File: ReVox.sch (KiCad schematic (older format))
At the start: 45 parts, among them CN1 EXPANSION_PORT, CN2 AUDIO_OUT, CN3 AUDIO_OUT, CN4 CN_RAW_DAC, U1 GAL20V8, U2 74LS273, U3 LM386

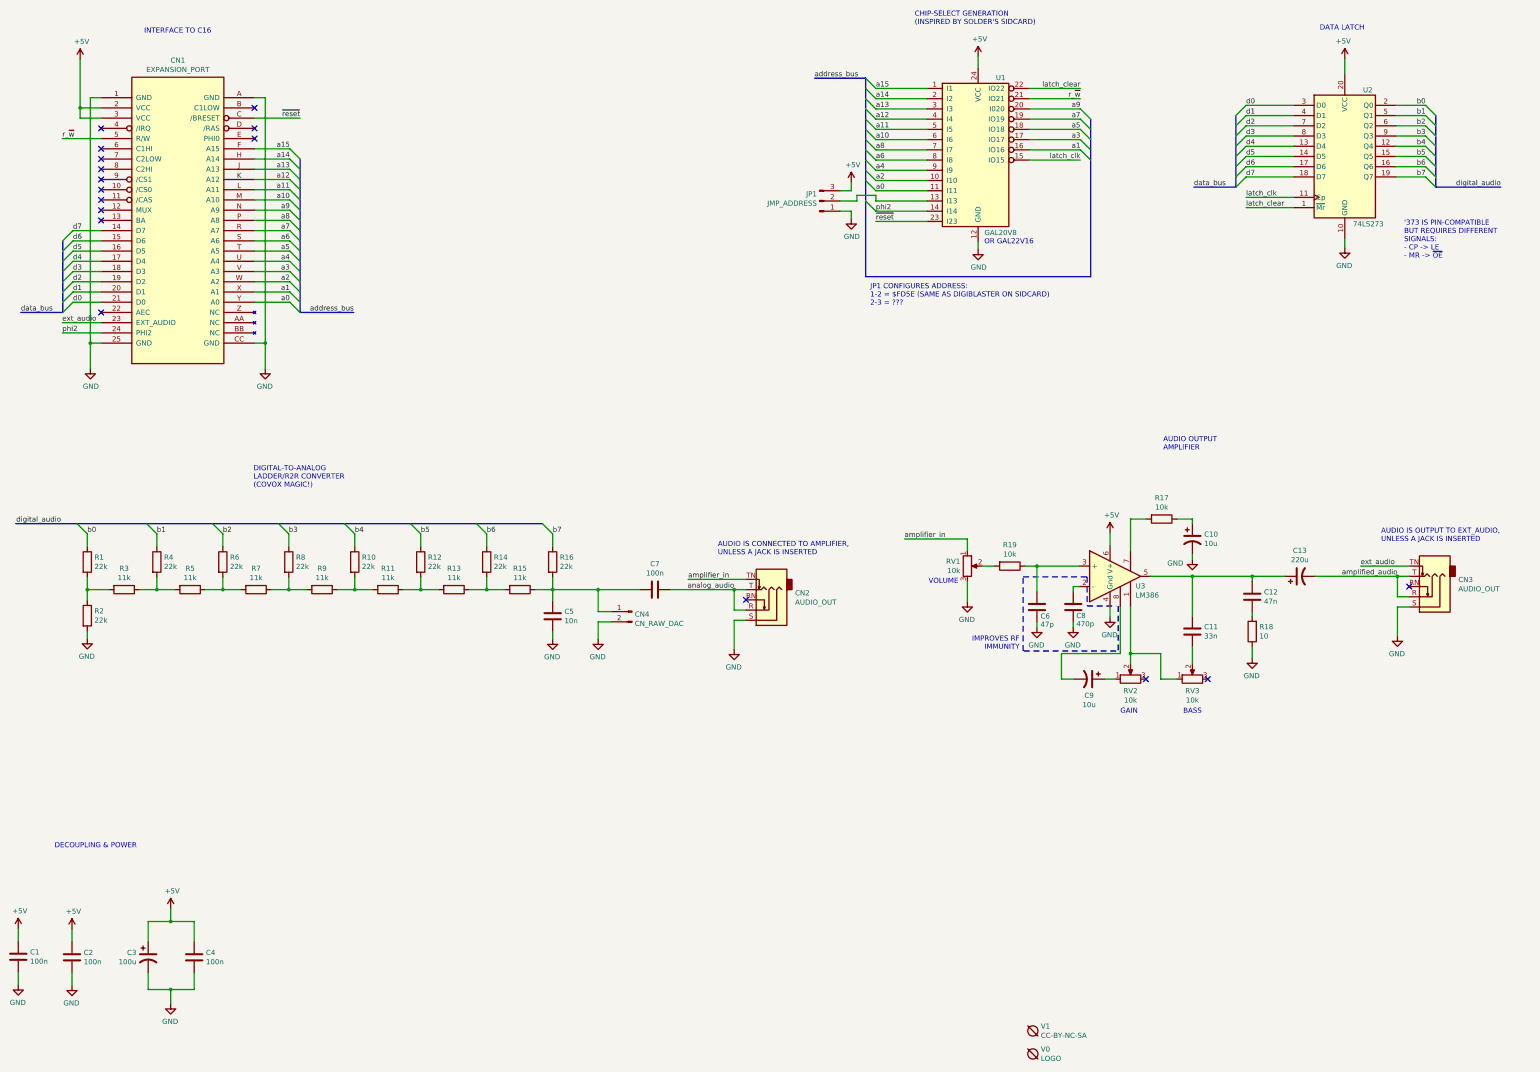
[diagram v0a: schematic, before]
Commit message: Simpler amplifier circuit
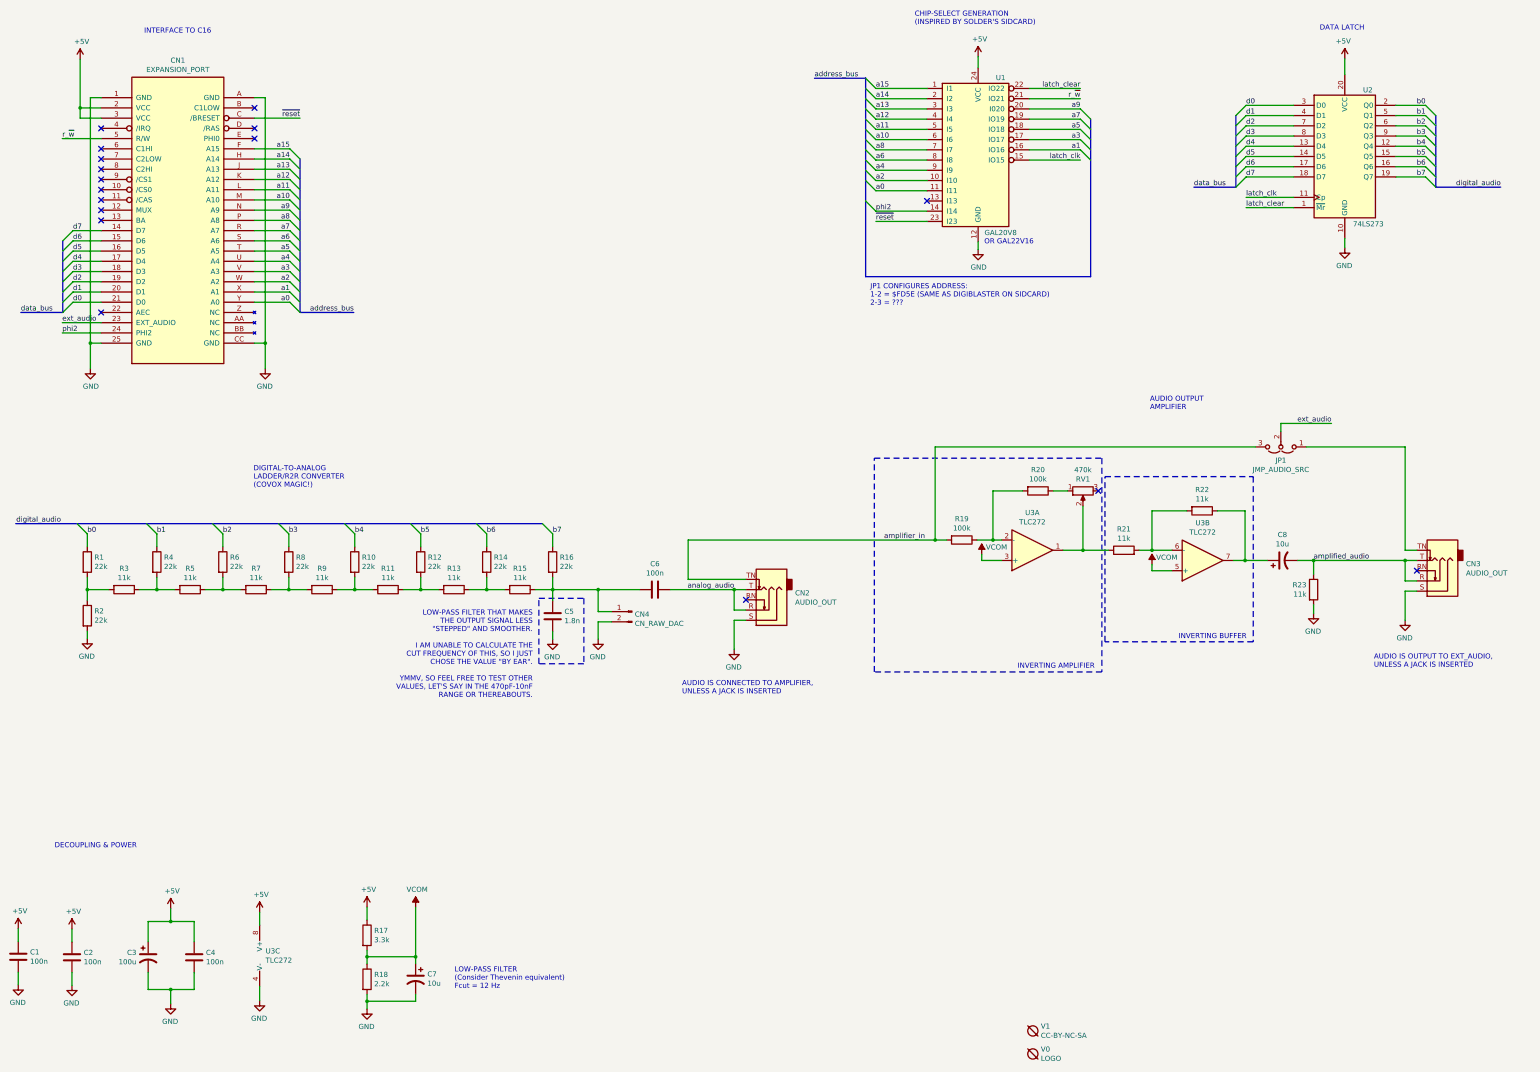
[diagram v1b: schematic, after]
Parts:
- removed C10, C9: 10u, Capacitor_THT:CP_Radial_D5.0mm_P2.00mm, symbol Device:CP1
- removed C11: 33n, Capacitor_THT:C_Disc_D7.0mm_W2.5mm_P5.00mm, symbol Device:C
- removed C12: 47n, Capacitor_THT:C_Disc_D7.0mm_W2.5mm_P5.00mm, symbol Device:C
- removed C13: 220u, Capacitor_THT:CP_Radial_D8.0mm_P3.50mm, symbol Device:CP1
- removed C6: 47p, Capacitor_THT:C_Disc_D7.0mm_W2.5mm_P5.00mm, symbol Device:C
- removed C8: 470p, Capacitor_THT:C_Disc_D7.0mm_W2.5mm_P5.00mm, symbol Device:C
- removed JP1: JMP_ADDRESS, Connector_PinHeader_2.54mm:PinHeader_1x03_P2.54mm_Vertical, symbol Connector:Conn_01x03_Male
- removed RV1, RV3: 10k, ReVox:Pot_Bourns_3306P, symbol Device:R_POT
- removed U3: LM386, Package_DIP:DIP-8_W7.62mm_Socket_LongPads, symbol lm386-mod-pin7:LM386
- added C7, C8: 10u, Capacitor_THT:CP_Radial_D5.0mm_P2.00mm, symbol Device:CP1
- added JP1: JMP_AUDIO_SRC, Jumper:SolderJumper-3_P1.3mm_Open_RoundedPad1.0x1.5mm, symbol Jumper:Jumper_3_Open
- added R20: 100k, Resistor_THT:R_Axial_DIN0207_L6.3mm_D2.5mm_P10.16mm_Horizontal, symbol Device:R
- added R21, R22, R23: 11k, Resistor_THT:R_Axial_DIN0207_L6.3mm_D2.5mm_P10.16mm_Horizontal, symbol Device:R
- added U3: TLC272, Package_DIP:DIP-8_W7.62mm_Socket_LongPads, symbol Amplifier_Operational:TLC272
- C5: value 10n -> 1.8n
- R17: value 10k -> 3.3k; MouserPN 603-MFR-25FTF52-10K -> (none); Notes Optional, can probably use 11K to reduce different parts co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 -> (none)
- R18: value 10 -> 2.2k; MouserPN 603-MFR-25FTE52-10R -> (none)
- R19: value 10k -> 100k; MouserPN 603-MFR-25FTF52-10K -> (none); Notes Optional, can probably use 11K to reduce different parts co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 -> (none)
- RV1: renamed from RV2; value 10k -> 470k
- renumbered C7 to C6
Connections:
- net +5V: now also R17.1, U3.8 (V+)
- net GND: now also R18.2, C7.2, R23.2, U3.4 (V-); no longer R18.1
- net amplified_audio: now also C8.2, R23.1
- net amplifier_in: now also R19.2, JP1.3 (B)
- net ext_audio: now also JP1.2 (C); no longer CN3.TN
- net at RV1.2: now also R21.1, U3.1
- net at R19.1: now also R20.2, U3.2 (-)
- net VCOM: now reaches R17.2
- net VCOM: now also R18.1, C7.1, U3.3 (+), U3.5 (+)
- net at RV1.1: now also R20.1
- new net: R21.2, R22.2, U3.6 (-)
- new net: C8.1, R22.1, U3.7
- new net: CN3.TN, JP1.1 (A)
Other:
- note added: "INVERTING AMPLIFIER"
- note added: "INVERTING BUFFER"
- note added: "LOW-PASS FILTER THAT MAKES\nTHE OUTPUT SIGNAL LESS\n"STEPPED" AND SMOOTHER.\n\nI AM UNABLE TO CALCULATE THE\nCUT FREQUENCY OF THIS, SO I JUST\nCHOSE THE VALUE "BY EAR".\n\nYMMV, SO FEEL FREE TO TEST OTHER\nVALUES, LET'S SAY IN THE 470pF-10nF\nRANGE OR THEREABOUTS."
- note added: "LOW-PASS FILTER\n(Consider Thevenin equivalent)\nFcut = 12 Hz"
- note removed: "'373 IS PIN-COMPATIBLE\nBUT REQUIRES DIFFERENT\nSIGNALS:\n- CP -> LE\n- MR -> ~OE~"
- note removed: "BASS"
- note removed: "GAIN"
- note removed: "IMPROVES RF\nIMMUNITY"
- note removed: "VOLUME"
- moved on the sheet: RV1

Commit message: Move some stuff
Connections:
- net at R21.1, RV1.2: now also U3.7; no longer U3.1
- net at R19.1, R20.2: now also U3.6 (-); no longer U3.2 (-)
- net at R21.2, R22.2: now also U3.2 (-); no longer U3.6 (-)
- net at C8.1, R22.1: now also U3.1; no longer U3.7
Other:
- moved on the sheet: U3A, U3B
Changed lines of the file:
@@
 L Amplifier_Operational:TLC272 U?
 U 1 1 65C5C5F8
-P 10995 6100
+P 12660 6200
 AR Path="/65BF4077/65C5C5F8" Ref="U?"  Part="1"
 AR Path="/65C5C5F8" Ref="U3"  Part="1"
-F 0 "U3" H 10995 5733 50  0000 C CNN
-F 1 "TLC272" H 10995 5824 50  0000 C CNN
-F 2 "Package_DIP:DIP-8_W7.62mm_Socket_LongPads" H 10995 6100 50  0001 C CNN
-F 3 "http://www.ti.com/lit/ds/symlink/tlc272.pdf" H 10995 6100 50  0001 C CNN
-	1    10995 6100
+F 0 "U3" H 12660 5833 50  0000 C CNN
+F 1 "TLC272" H 12660 5924 50  0000 C CNN
+F 2 "Package_DIP:DIP-8_W7.62mm_Socket_LongPads" H 12660 6200 50  0001 C CNN
+F 3 "http://www.ti.com/lit/ds/symlink/tlc272.pdf" H 12660 6200 50  0001 C CNN
+	1    12660 6200
 	1    0    0    1
 $EndComp
@@
 L Amplifier_Operational:TLC272 U?
 U 2 1 65C5C5FE
-P 12660 6200
+P 10995 6100
 AR Path="/65BF4077/65C5C5FE" Ref="U?"  Part="2"
 AR Path="/65C5C5FE" Ref="U3"  Part="2"
-F 0 "U3" H 12660 5833 50  0000 C CNN
-F 1 "TLC272" H 12660 5924 50  0000 C CNN
-F 2 "Package_DIP:DIP-8_W7.62mm_Socket_LongPads" H 12660 6200 50  0001 C CNN
-F 3 "http://www.ti.com/lit/ds/symlink/tlc272.pdf" H 12660 6200 50  0001 C CNN
-	2    12660 6200
+F 0 "U3" H 10995 5733 50  0000 C CNN
+F 1 "TLC272" H 10995 5824 50  0000 C CNN
+F 2 "Package_DIP:DIP-8_W7.62mm_Socket_LongPads" H 10995 6100 50  0001 C CNN
+F 3 "http://www.ti.com/lit/ds/symlink/tlc272.pdf" H 10995 6100 50  0001 C CNN
+	2    10995 6100
 	1    0    0    1
 $EndComp

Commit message: Routing done
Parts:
- R21, R22: value 11k -> 100k
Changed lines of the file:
@@
 AR Path="/65BF4077/65C5C654" Ref="R?"  Part="1"
 F 0 "R22" V 12448 5715 50  0000 C CNN
-F 1 "11k" V 12539 5715 50  0000 C CNN
+F 1 "100k" V 12539 5715 50  0000 C CNN
 F 2 "Resistor_THT:R_Axial_DIN0207_L6.3mm_D2.5mm_P10.16mm_Horizontal" V 12585 5715 50  0001 C CNN
 F 3 "~" H 12655 5715 50  0001 C CNN
@@
 AR Path="/65BF4077/65C5C65B" Ref="R?"  Part="1"
 F 0 "R21" V 12097 6100 50  0000 C CNN
-F 1 "11k" V 12006 6100 50  0000 C CNN
+F 1 "100k" V 12006 6100 50  0000 C CNN
 F 2 "Resistor_THT:R_Axial_DIN0207_L6.3mm_D2.5mm_P10.16mm_Horizontal" V 11820 6100 50  0001 C CNN
 F 3 "~" H 11890 6100 50  0001 C CNN
@@
 Wire Wire Line
 	14640 5090 14640 6100
-$Comp
-L Jumper:Jumper_3_Open JP?
-U 1 1 65C5C692
-P 13425 5090
-AR Path="/65BF4077/65C5C692" Ref="JP?"  Part="1"
-AR Path="/65C5C692" Ref="JP1"  Part="1"
-F 0 "JP1" H 13425 5221 50  0000 C CNN
-F 1 "JMP_AUDIO_SRC" H 13425 5312 50  0000 C CNN
-F 2 "Jumper:SolderJumper-3_P1.3mm_Open_RoundedPad1.0x1.5mm" H 13425 5090 50  0001 C CNN
-F 3 "~" H 13425 5090 50  0001 C CNN
-	1    13425 5090
-	-1   0    0    1
-$EndComp
 $Comp
 L Amplifier_Operational:TLC272 U3
@@
 	11565 1885 11565 3425
 Wire Bus Line
+	1055 5840 6205 5840
+Wire Bus Line
+	12985 1850 12985 2550
+Wire Bus Line
+	14940 1850 14940 2550
+Wire Bus Line
+	9365 1480 9365 3425
+Wire Bus Line
 	1515 3075 1515 3775
 Wire Bus Line
-	14940 1850 14940 2550
-Wire Bus Line
-	12985 1850 12985 2550
-Wire Bus Line
-	1055 5840 6205 5840
-Wire Bus Line
 	3835 2275 3835 3775
-Wire Bus Line
-	9365 1480 9365 3425
+$Comp
+L Jumper:Jumper_3_Open JP?
+U 1 1 65C5C692
+P 13425 5090
+AR Path="/65BF4077/65C5C692" Ref="JP?"  Part="1"
+AR Path="/65C5C692" Ref="JP1"  Part="1"
+F 0 "JP1" H 13425 5221 50  0000 C CNN
+F 1 "JMP_AUDIO_SRC" H 13425 5312 50  0000 C CNN
+F 2 "Jumper:SolderJumper-3_P1.3mm_Open_RoundedPad1.0x1.5mm" H 13425 5090 50  0001 C CNN
+F 3 "~" H 13425 5090 50  0001 C CNN
+	1    13425 5090
+	-1   0    0    1
+$EndComp
 $EndSCHEMATC

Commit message: Final touches
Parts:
- C5: Notes Optional, filters DAC output -> DAC output low-pass filter, goes to taste in the 470pF-10nF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
- C7, C8: MouserPN (none) -> 710-860010572002
- CN2: value AUDIO_OUT -> RAW_OUT
- CN3: value AUDIO_OUT -> AMP_OUT
- CN4: MouserPN (none) -> -; Notes (none) -> Mainly meant for debugging
- JP1: MouserPN (none) -> -
- R1, R10, R12, R14, R16, R2, R4, R6, R8: Notes (none) -> Exact value is not critical as long as it is exactly TWICE 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
- R11, R13, R15, R3, R5, R7, R9: Notes (none) -> Exact value is not critical as long as it is exactly HALF R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
- R19, R20: MouserPN (none) -> 603-MFR-25FTE52-11K; Notes (none) -> 1% or better
- R21, R22: Notes (none) -> 1% or better
- R23: value 11k -> 10k
- RV1: MouserPN 652-3306P-1-103 -> (none); Notes Skip if Gain control is not desired -> (none)
- U3: MouserPN (none) -> 595-TLC272BIP
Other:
- note removed: "JP1 CONFIGURES ADDRESS:\n1-2 = $FD5E (SAME AS DIGIBLASTER ON SIDCARD)\n2-3 = ???"

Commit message: RV1 -> 500k
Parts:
- RV1: value 470k -> 500k; MouserPN (none) -> 652-3306P-1-504
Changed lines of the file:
@@
 P 11490 5520
 F 0 "RV1" V 11375 5520 50  0000 C CNN
-F 1 "470k" V 11284 5520 50  0000 C CNN
+F 1 "500k" V 11284 5520 50  0000 C CNN
 F 2 "ReVox:Pot_Bourns_3306P" H 11490 5520 50  0001 C CNN
 F 3 "~" H 11490 5520 50  0001 C CNN
-F 4 "" H 11490 5520 50  0001 C CNN "MouserPN"
+F 4 "652-3306P-1-504" H 11490 5520 50  0001 C CNN "MouserPN"
 F 5 "" H 11490 5520 50  0001 C CNN "Notes"
 	1    11490 5520

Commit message: C8 -> 1uF
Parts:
- C8: value 10u -> 1u; MouserPN 710-860010572002 -> 710-860010672005
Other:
- note added: "C6 FORMS A HIGH-PASS\nFILTER WITH R19 WHEN\nAUDIO GOES TO AMPLIFIER\n\nFcut ~~= 16 Hz"
- note added: "HIGH-PASS FILTER\n\nFcut ~~= 16 Hz"
- note added: "LOW-PASS FILTER THAT MAKES\nTHE OUTPUT SIGNAL LESS\n"STEPPED" AND SMOOTHER.\n\nI AM UNABLE TO CALCULATE THE\nCUT FREQUENCY OF THIS, SO I JUST\nCHOSE THE VALUE "BY EAR". BUT IF\nI UNDERSTAND CORRECTLY, THE\nOUTPUT IMPEDANCE OF AN R-2R\nNETWORK IS JUST R, SO WITH R=11k\nAND C5 = 1.8n, Fcut ~~= 8 kHz.\n680p AND 820p WOULD SET IT AT\n21277 AND 17644 Hz RESPECTIVELY.\n\nYMMV, SO FEEL FREE TO TEST OTHE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"
- note removed: "LOW-PASS FILTER THAT MAKES\nTHE OUTPUT SIGNAL LESS\n"STEPPED" AND SMOOTHER.\n\nI AM UNABLE TO CALCULATE THE\nCUT FREQUENCY OF THIS, SO I JUST\nCHOSE THE VALUE "BY EAR".\n\nYMMV, SO FEEL FREE TO TEST OTHER\nVALUES, LET'S SAY IN THE 470pF-10nF\nRANGE OR THEREABOUTS."
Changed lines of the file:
@@
 Sheet 1 1
 Title "ReVox"
-Date "2023-09-24"
+Date "2023-10-29"
 Rev "1git"
 Comp "SukkoPera"
 Comment1 "Based on work by Yeo Kheng Meng"
-Comment2 "Amplifier circuit by Scott Campbell"
-Comment3 "Licensed under CC BY-NC-SA 4.0"
+Comment2 "Licensed under CC BY-NC-SA 4.0"
+Comment3 ""
 Comment4 ""
 $EndDescr
@@
 Wire Wire Line
 	9965 2785 9465 2785
-Entry Wire Line
-	9365 2685 9465 2785
 Wire Wire Line
 	9965 2885 9465 2885
@@
 $EndComp
 Wire Wire Line
-	8195 6385 7630 6385
+	8195 6385 8080 6385
 Wire Wire Line
 	8080 6485 8195 6485
@@
 AR Path="/65BF4077/65C5C61C" Ref="C?"  Part="1"
 F 0 "C8" V 13692 6200 50  0000 C CNN
-F 1 "10u" V 13601 6200 50  0000 C CNN
+F 1 "1u" V 13601 6200 50  0000 C CNN
 F 2 "Capacitor_THT:CP_Radial_D5.0mm_P2.00mm" H 13440 6200 50  0001 C CNN
 F 3 "~" H 13440 6200 50  0001 C CNN
-F 4 "710-860010572002" H 13440 6200 50  0001 C CNN "MouserPN"
+F 4 "710-860010672005" H 13440 6200 50  0001 C CNN "MouserPN"
 	1    13440 6200
 	0    -1   -1   0
@@
 $EndComp
 Wire Wire Line
-	7630 6385 7630 6000
-Wire Wire Line
-	7630 6000 10045 6000
+	8080 6385 8080 6000
+Wire Wire Line
+	8080 6000 10045 6000
 $Comp
 L power:+5V #PWR?
@@
 	13745 6200 14640 6200
 Connection ~ 13745 6200
-Text Notes 6110 7550 2    50   ~ 0
-LOW-PASS FILTER THAT MAKES\nTHE OUTPUT SIGNAL LESS\n"STEPPED" AND SMOOTHER.\n\nI AM UNABLE TO CALCULATE THE\nCUT FREQUENCY OF THIS, SO I JUST\nCHOSE THE VALUE "BY EAR".\n\nYMMV, SO FEEL FREE TO TEST OTHER\nVALUES, LET'S SAY IN THE 470pF-10nF\nRANGE OR THEREABOUTS.
+Text Notes 6095 8085 2    50   ~ 0
+LOW-PASS FILTER THAT MAKES\nTHE OUTPUT SIGNAL LESS\n"STEPPED" AND SMOOTHER.\n\nI AM UNABLE TO CALCULATE THE\nCUT FREQUENCY OF THIS, SO I JUST\nCHOSE THE VALUE "BY EAR". BUT IF\nI UNDERSTAND CORRECTLY, THE\nOUTPUT IMPEDANCE OF AN R-2R\nNETWORK IS JUST R, SO WITH R=11k\nAND C5 = 1.8n, Fcut ~~= 8 kHz.\n680p AND 820p WOULD SET IT AT\n21277 AND 17644 Hz RESPECTIVELY.\n\nYMMV, SO FEEL FREE TO TEST OTHER\nVALUES, LET'S SAY IN THE 470pF-10nF\nRANGE OR THEREABOUTS.\n\n
 Wire Notes Line
 	6170 6570 6610 6570
@@
 	-1   0    0    1
 $EndComp
+Text Notes 7760 6105 2    50   ~ 0
+C6 FORMS A HIGH-PASS\nFILTER WITH R19 WHEN\nAUDIO GOES TO AMPLIFIER\n\nFcut ~~= 16 Hz
+Wire Notes Line
+	13215 5800 13975 5800
+Wire Notes Line
+	13975 5800 13975 6995
+Wire Notes Line
+	13975 6995 13215 6995
+Wire Notes Line
+	13215 6995 13215 5800
 Wire Bus Line
 	11565 1885 11565 3425
@@
 Wire Bus Line
 	9365 1480 9365 3425
+Text Notes 13225 7290 0    50   ~ 0
+HIGH-PASS FILTER\n\nFcut ~~= 16 Hz
 $EndSCHEMATC

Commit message: Add a few notes on schematics
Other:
- note added: "- WARNING -\nAMPLIFIER SEEMS TO\nOSCILLATE WHEN\nTHIS JACK IS USED"
- note added: "This is the bias voltage for the opamp.\nIt is set at +2V because the TLC272\nswings between 0 and 4V. If using a\nrail-to-rail opamp (like the LMC6482,\nfor instance), this can be set at 2.5V\nby using the same value for R17 and\nR18 (hint: 11k works fine if already\nused for the resistor ladder)."
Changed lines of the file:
@@
 	-1   0    0    -1
 $EndComp
-Text Notes 5345 10395 0    50   ~ 0
+Text Notes 4785 10825 0    50   ~ 0
 LOW-PASS FILTER\n(Consider Thevenin equivalent)\nFcut = 12 Hz
 $Comp
@@
 Wire Notes Line
 	13215 6995 13215 5800
+Text Notes 13225 7290 0    50   ~ 0
+HIGH-PASS FILTER\n\nFcut ~~= 16 Hz
+Text Notes 14785 5880 0    50   ~ 0
+- WARNING -\nAMPLIFIER SEEMS TO\nOSCILLATE WHEN\nTHIS JACK IS USED
+Text Notes 5125 10120 0    50   ~ 0
+This is the bias voltage for the opamp.\nIt is set at +2V because the TLC272\nswings between 0 and 4V. If using a\nrail-to-rail opamp (like the LMC6482,\nfor instance), this can be set at 2.5V\nby using the same value for R17 and\nR18 (hint: 11k works fine if already\nused for the resistor ladder).
 Wire Bus Line
 	11565 1885 11565 3425
@@
 Wire Bus Line
 	9365 1480 9365 3425
-Text Notes 13225 7290 0    50   ~ 0
-HIGH-PASS FILTER\n\nFcut ~~= 16 Hz
 $EndSCHEMATC
